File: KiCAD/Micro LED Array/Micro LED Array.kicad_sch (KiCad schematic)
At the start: 32 parts

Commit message: 56 strip 2
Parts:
- added D33, D34, D35, D36, D37, D38, D39, D40, D41, D42, D43, D44, D45, D46, D47, D48, D49, D50, D51, D52, D53, D54, D55, D56: LED, Custom footprints:LED_APG0603SEC-E-TT_KNB, symbol Device:LED
- renumbered D15 to D10, D14 to D11, D13 to D12, D12 to D13, D11 to D14, D10 to D15, D9 to D16, D32 to D25, D31 to D26, D30 to D27, D29 to D28, D28 to D29, D27 to D30, D26 to D31, D25 to D32, D16 to D9
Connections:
- net GND: now also D56.1 (K); no longer D25.1 (K)
- new net: D41.2 (A), D42.1 (K)
- new net: D42.2 (A), D43.1 (K)
- new net: D43.2 (A), D44.1 (K)
- new net: D46.2 (A), D47.1 (K)
- new net: D47.2 (A), D48.1 (K)
- new net: D53.1 (K), D54.2 (A)
- new net: D52.1 (K), D53.2 (A)
- new net: D44.2 (A), D45.1 (K)
- new net: D45.2 (A), D46.1 (K)
- new net: D40.1 (K), D48.2 (A)
- new net: D39.1 (K), D40.2 (A)
- new net: D51.1 (K), D52.2 (A)
- new net: D50.1 (K), D51.2 (A)
- new net: D49.1 (K), D50.2 (A)
- new net: D41.1 (K), D49.2 (A)
- new net: D55.1 (K), D56.2 (A)
- new net: D54.1 (K), D55.2 (A)
- new net: D38.1 (K), D39.2 (A)
- new net: D36.1 (K), D37.2 (A)
- new net: D35.1 (K), D36.2 (A)
- new net: D25.1 (K), D33.2 (A)
- new net: D33.1 (K), D34.2 (A)
- new net: D37.1 (K), D38.2 (A)
- new net: D34.1 (K), D35.2 (A)
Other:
- moved on the sheet: D1, D10, D11, D12, D13, D14, D15, D16, D17, D18, D19, D2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

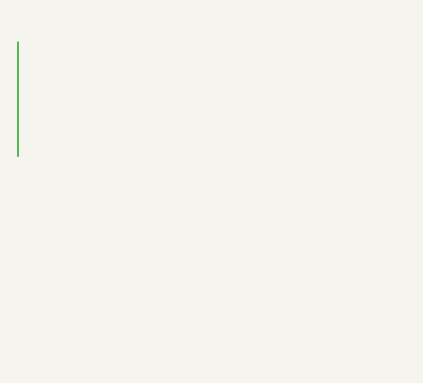
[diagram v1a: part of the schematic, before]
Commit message: Add bodge pads to diagnose and bypass LEDs
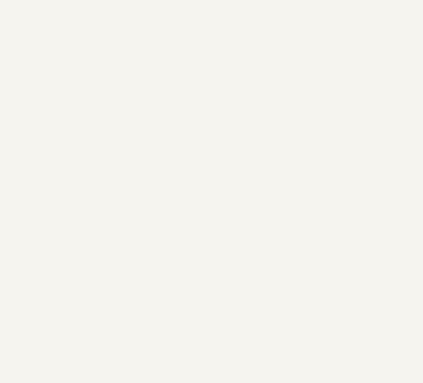
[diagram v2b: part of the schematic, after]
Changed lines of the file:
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@@
-    (stroke (width 0) (type default))
-  )
-  (wire (pts (xy 21.59 54.61) (xy 21.59 67.31))
     (stroke (width 0) (type default))
   )

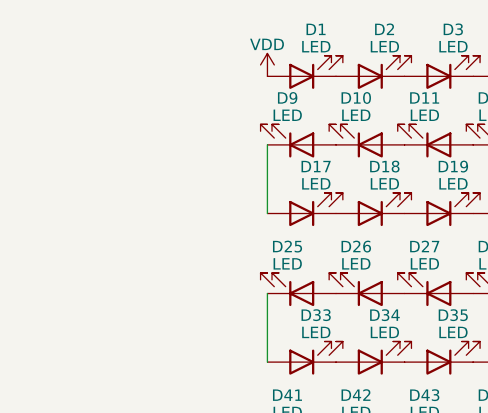
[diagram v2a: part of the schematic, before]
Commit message: Add fuses, RS232, Vref, Vsense, Isense
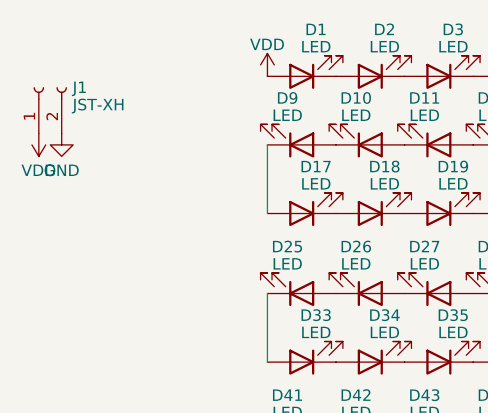
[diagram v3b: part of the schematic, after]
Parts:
- added J1: JST-XH, Custom footprints:JST_B2B-XH-A, symbol Connector:Conn_01x02_Socket
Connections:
- net GND: now also J1.2 (Pin_2)
- net VDD: now also J1.1 (Pin_1)
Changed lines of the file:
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@@
+    )
+  )
+  (symbol (lib_id "power:GND") (at 67.31 64.77 0) (unit 1)
+    (in_bom yes) (on_board yes) (dnp no) (fields_autoplaced)
+    (property "Reference" "#PWR04" (at 67.31 71.12 0)
+      (effects (font (size 1.27 1.27)) hide)
+    )
+    (property "Value" "GND" (at 67.31 68.9055 0)
+      (effects (font (size 1.27 1.27)))
+    )
+    (property "Footprint" "" (at 67.31 64.77 0)
+      (effects (font (size 1.27 1.27)) hide)
+    )
+    (property "Datasheet" "" (at 67.31 64.77 0)
+      (effects (font (size 1.27 1.27)) hide)
+    )
+    (pin "1")
+    (instances
+      (project "Micro LED Array"
+        (path "/501b6f31-167f-4148-be11-c5bed0bfbf7d"
+          (reference "#PWR04") (unit 1)
+        )
+      )
     )
   )
@@
     )
   )
+  (symbol (lib_id "power:VDD") (at 64.77 64.77 180) (unit 1)
+    (in_bom yes) (on_board yes) (dnp no) (fields_autoplaced)
+    (property "Reference" "#PWR03" (at 64.77 60.96 0)
+      (effects (font (size 1.27 1.27)) hide)
+    )
+    (property "Value" "VDD" (at 64.77 68.9055 0)
+      (effects (font (size 1.27 1.27)))
+    )
+    (property "Footprint" "" (at 64.77 64.77 0)
+      (effects (font (size 1.27 1.27)) hide)
+    )
+    (property "Datasheet" "" (at 64.77 64.77 0)
+      (effects (font (size 1.27 1.27)) hide)
+    )
+    (pin "1")
+    (instances
+      (project "Micro LED Array"
+        (path "/501b6f31-167f-4148-be11-c5bed0bfbf7d"
+          (reference "#PWR03") (unit 1)
+        )
+      )
+    )
+  )
   (symbol (lib_id "Device:LED") (at 132.08 99.06 0) (mirror x) (unit 1)
     (in_bom yes) (on_board yes) (dnp no) (fields_autoplaced)
@@
         )
       )
+    )
+  )
+  (symbol (lib_id "Connector:Conn_01x02_Socket") (at 64.77 59.69 90) (unit 1)
+    (in_bom yes) (on_board yes) (dnp no) (fields_autoplaced)
+    (property "Reference" "J1" (at 68.5292 59.6813 90)
+      (effects (font (size 1.27 1.27)) (justify right))
+    )
+    (property "Value" "JST-XH" (at 68.5292 61.6023 90)
+      (effects (font (size 1.27 1.27)) (justify right))
+    )
+    (property "Footprint" "Custom footprints:JST_B2B-XH-A" (at 64.77 59.69 0)
+      (effects (font (size 1.27 1.27)) hide)
+    )
+    (property "Datasheet" "https://www.jst-mfg.com/product/pdf/eng/eXH.pdf" (at 64.77 59.69 0)
+      (effects (font (size 1.27 1.27)) hide)
+    )
+    (property "Manufacturer" "JST Sales America Inc." (at 64.77 59.69 0)
+      (effects (font (size 1.27 1.27)) hide)
+    )
+    (property "Part" "B2B-XH-A" (at 64.77 59.69 0)
+      (effects (font (size 1.27 1.27)) hide)
+    )
+    (pin "1")
+    (pin "2")
+    (instances
+      (project "Micro LED Array"
+        (path "/501b6f31-167f-4148-be11-c5bed0bfbf7d"
+          (reference "J1") (unit 1)
+        )
+      )

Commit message: Current setup
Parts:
- removed D13, D14, D15, D16, D5, D6, D7, D8: LED, Custom footprints:LED_APG0603SEC-E-TT_KNB, symbol Device:LED
- J1: footprint Custom footprints:JST_B2B-XH-A -> Connector_Wire:SolderWire-0.1sqmm_1x02_P3.6mm_D0.4mm_OD1mm
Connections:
- net VDD: now also D4.2 (A); no longer D1.2 (A)
- net at D4.1 (K): now also D3.2 (A)
- net at D3.1 (K): now also D2.2 (A); no longer D4.2 (A)
- net at D12.2 (A): now also D1.1 (K)
- net at D2.1 (K): now also D1.2 (A); no longer D3.2 (A)
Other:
- note added: "44 LED String"
